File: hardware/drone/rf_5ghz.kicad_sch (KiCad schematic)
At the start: 25 parts, among them J5 Conn_01x06_Pin, U23 MM8030_2610RJ3, U7 CC3350, U8 DPX167125DT-8197B1, U9 DEA162450BT-1295A1, Y1 Crystal_GND24

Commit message: Added chip antenna footprint
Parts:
- AE1: footprint (none) -> SoftDroneLibrary:ANT-DB1-NSP250-T
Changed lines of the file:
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@@
 			)
 		)
-		(property "Footprint" ""
+		(property "Footprint" "SoftDroneLibrary:ANT-DB1-NSP250-T"
 			(at 163.83 157.48 0)
 			(hide yes)

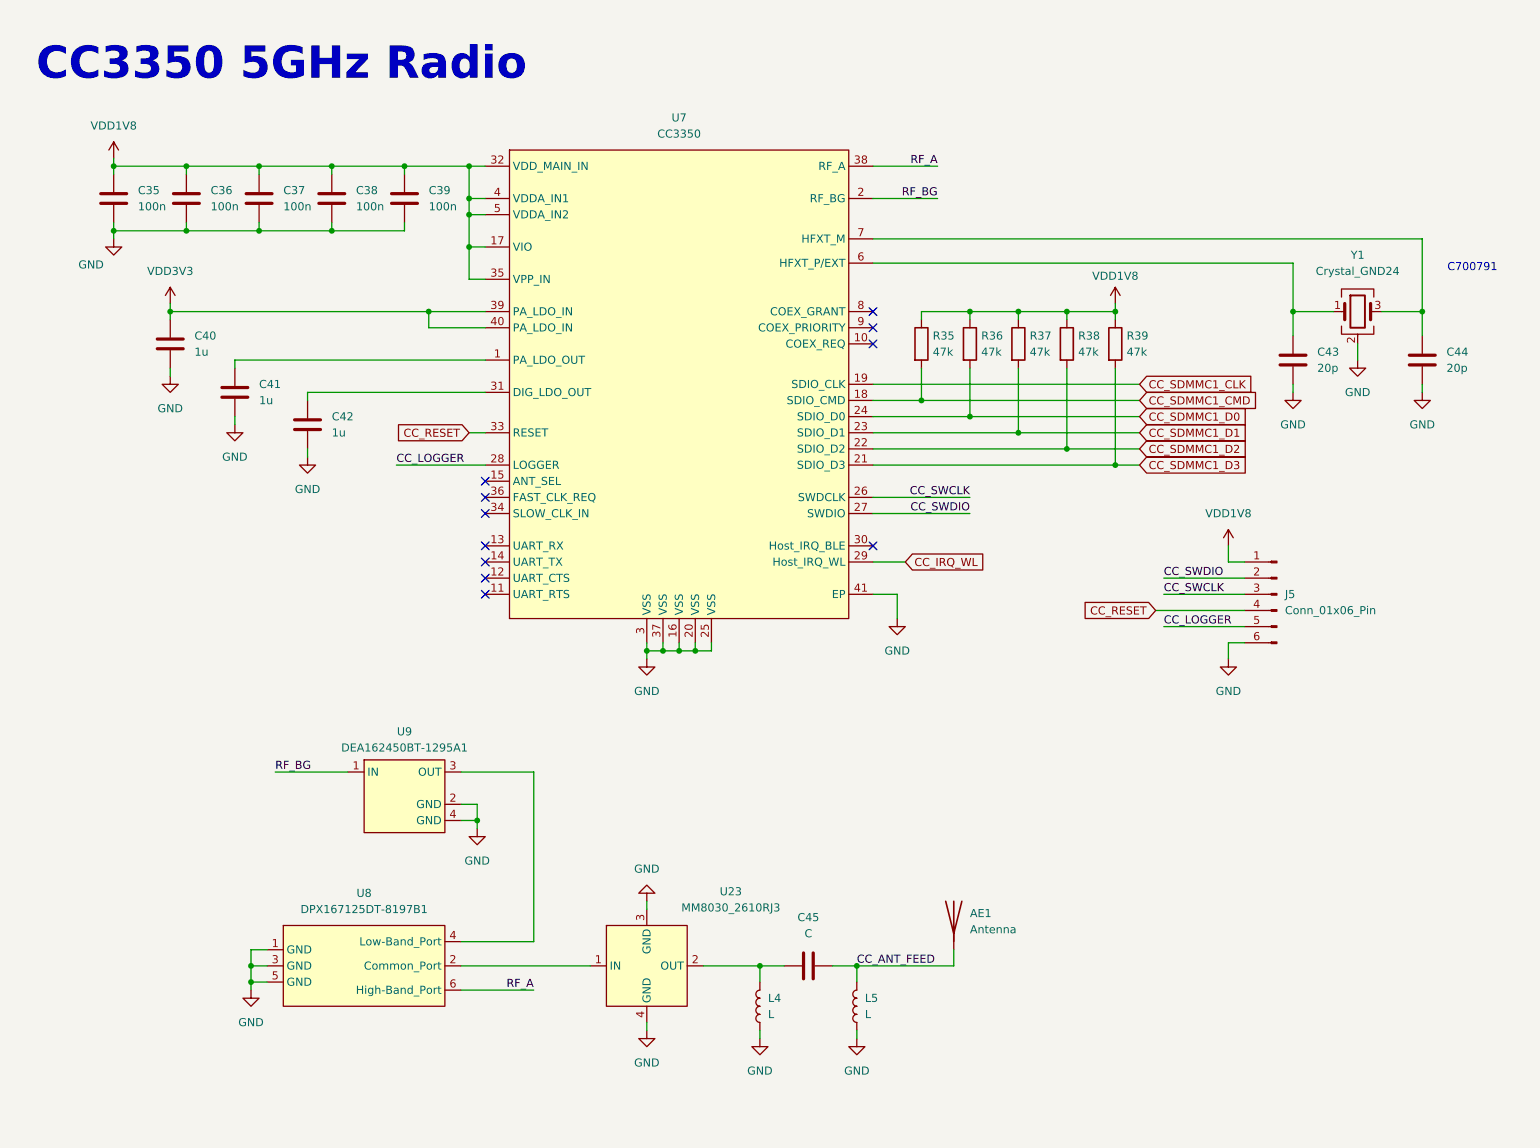
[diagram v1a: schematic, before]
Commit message: Labeled nets, added colours, and fixed stm32n6 schematic symbol issues
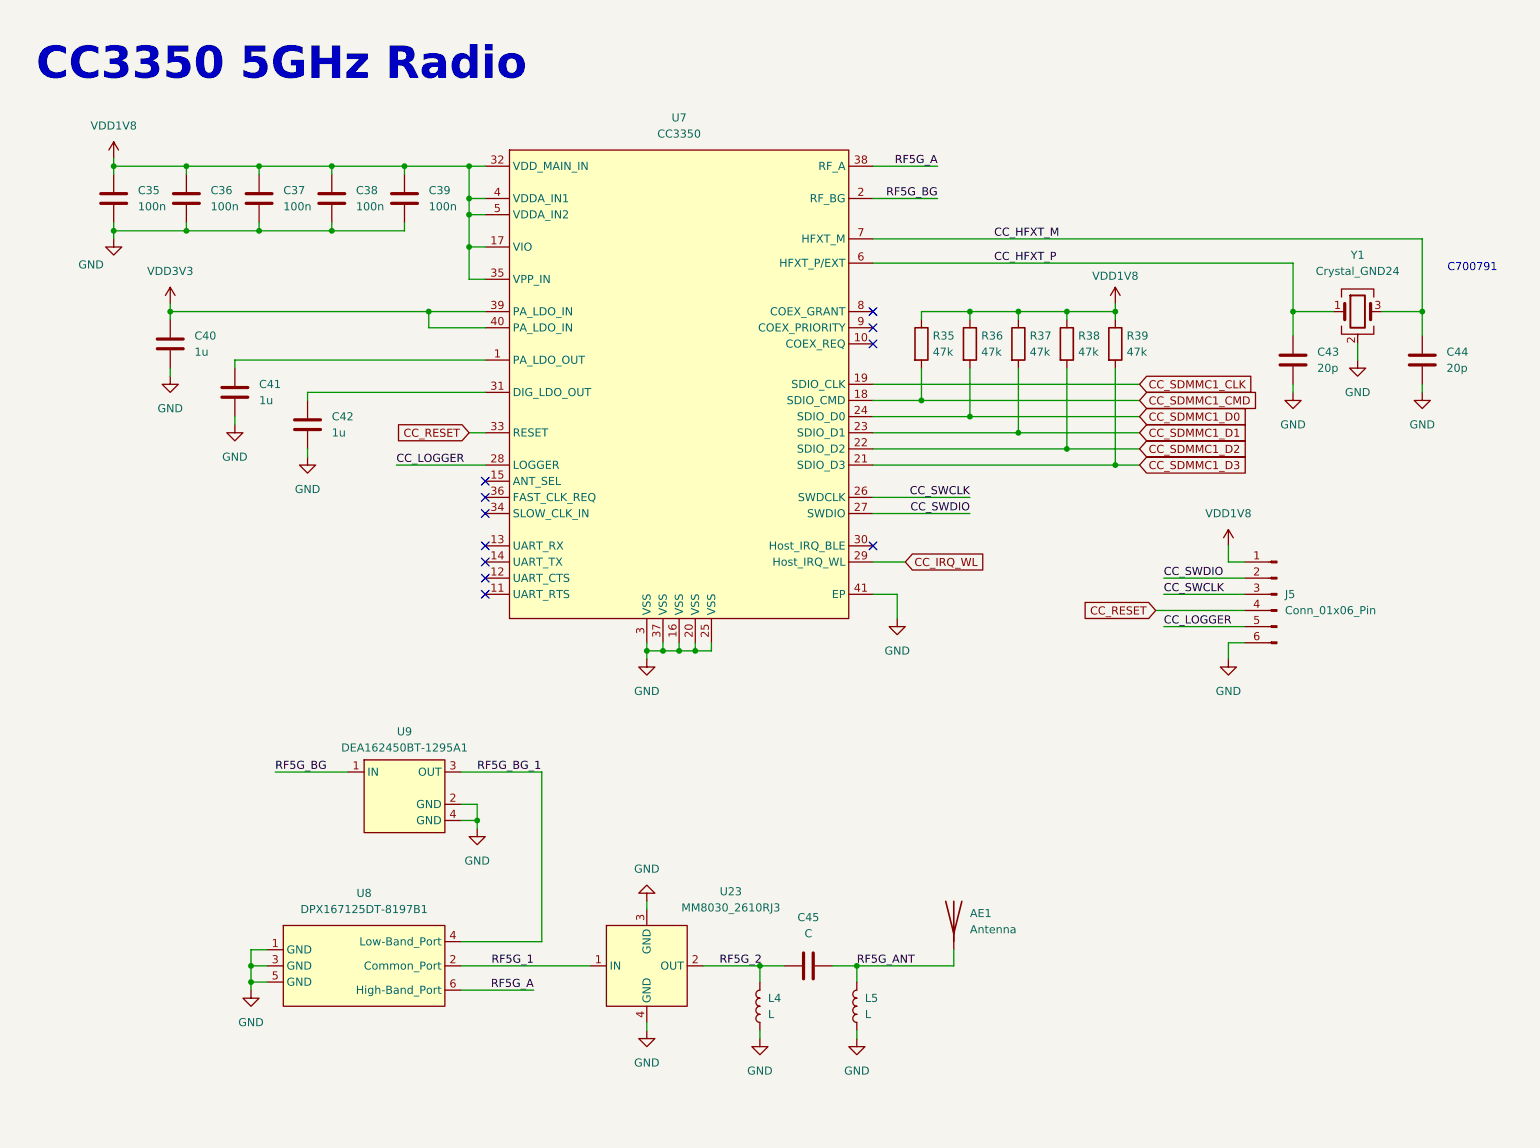
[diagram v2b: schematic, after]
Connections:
- net RF5G_BG_1: now reaches U8.4 (Low-Band_Port), U9.3 (OUT)
- net CC_HFXT_P: now reaches C43.1, U7.6 (HFXT_P/EXT), Y1.1
- net CC_HFXT_M: now reaches C44.1, U7.7 (HFXT_M), Y1.3
- net RF5G_2: now reaches C45.1, L4.2, U23.2 (OUT)
- net RF5G_1: now reaches U23.1 (IN), U8.2 (Common_Port)
- net CC_ANT_FEED renamed RF5G_ANT
- net RF_A renamed RF5G_A
- net RF_BG renamed RF5G_BG
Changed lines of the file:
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@@
 	(wire
 		(pts
-			(xy 86.36 134.62) (xy 97.79 134.62)
+			(xy 86.36 134.62) (xy 99.06 134.62)
 		)
 		(stroke
@@
 	(wire
 		(pts
-			(xy 97.79 134.62) (xy 97.79 161.29)
+			(xy 99.06 134.62) (xy 99.06 161.29)
 		)
 		(stroke
@@
 	(wire
 		(pts
-			(xy 97.79 161.29) (xy 86.36 161.29)
+			(xy 99.06 161.29) (xy 86.36 161.29)
 		)
 		(stroke
@@
 		)
 	)
-	(label "RF_A"
+	(label "CC_HFXT_M"
+		(at 170.18 50.8 0)
+		(effects
+			(font
+				(size 1.27 1.27)
+			)
+			(justify left bottom)
+		)
+	)
+	(label "RF5G_A"
 		(at 97.79 168.91 180)
 		(effects
@@
 		)
 	)
-	(label "RF_BG"
+	(label "RF5G_BG"
 		(at 161.29 44.45 180)
 		(effects
@@
 			)
 			(justify right bottom)
+		)
+	)
+	(label "RF5G_2"
+		(at 127 165.1 0)
+		(effects
+			(font
+				(size 1.27 1.27)
+			)
+			(justify left bottom)
+		)
+	)
+	(label "CC_HFXT_P"
+		(at 170.18 54.61 0)
+		(effects
+			(font
+				(size 1.27 1.27)
+			)
+			(justify left bottom)
 		)
 	)
@@
 		)
 	)
-	(label "CC_ANT_FEED"
+	(label "RF5G_BG_1"
+		(at 88.9 134.62 0)
+		(effects
+			(font
+				(size 1.27 1.27)
+			)
+			(justify left bottom)
+		)
+	)
+	(label "RF5G_ANT"
 		(at 148.59 165.1 0)
 		(effects
@@
 		)
 	)
-	(label "RF_A"
+	(label "RF5G_A"
 		(at 161.29 39.37 180)
+		(effects
+			(font
+				(size 1.27 1.27)
+			)
+			(justify right bottom)
+		)
+	)
+	(label "RF5G_1"
+		(at 97.79 165.1 180)
 		(effects
 			(font
@@
 		)
 	)
-	(label "RF_BG"
+	(label "RF5G_BG"
 		(at 57.15 134.62 0)
 		(effects

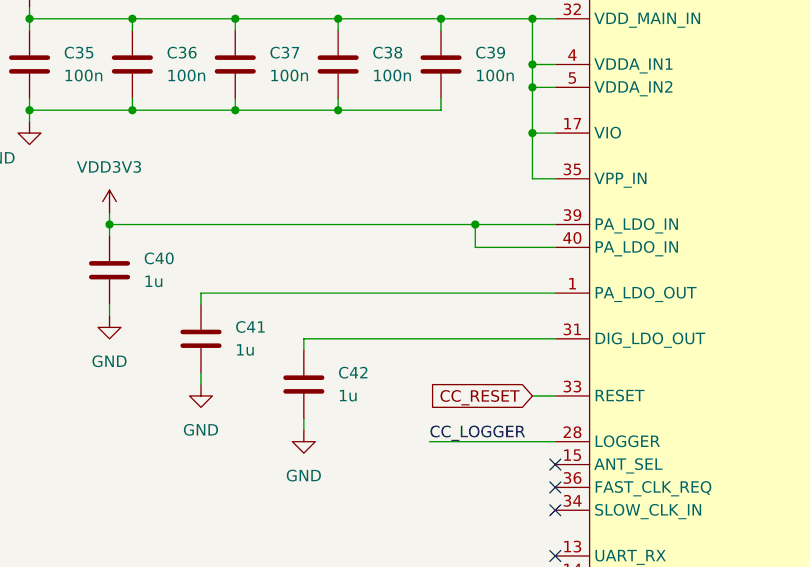
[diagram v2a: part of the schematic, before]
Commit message: Started layout and tested RF routing paths
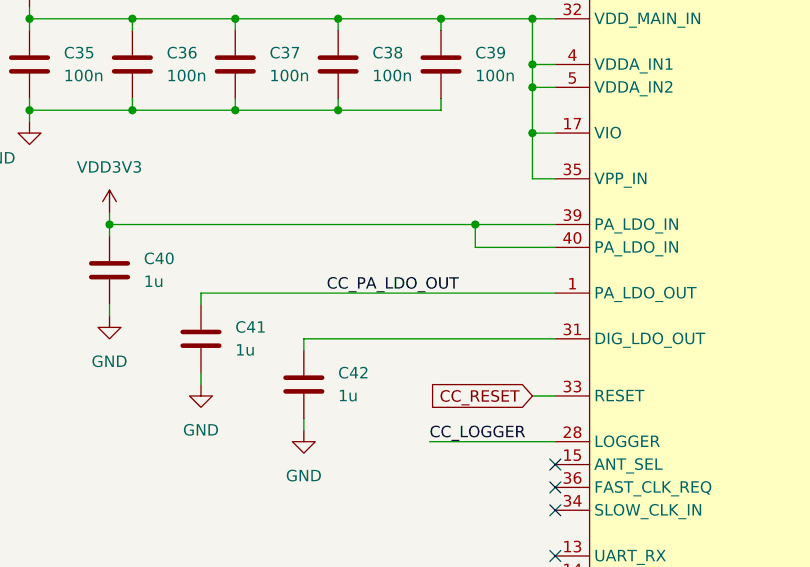
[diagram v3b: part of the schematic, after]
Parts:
- C45: footprint Capacitor_SMD:C_0402_1005Metric -> Capacitor_SMD:C_0603_1608Metric
- L4, L5: footprint Inductor_SMD:L_0402_1005Metric -> Inductor_SMD:L_0603_1608Metric
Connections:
- net CC_PA_LDO_OUT: now reaches C41.1, U7.1 (PA_LDO_OUT)
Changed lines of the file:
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@@
+		)
+	)
+	(label "CC_PA_LDO_OUT"
+		(at 64.77 69.85 0)
+		(effects
+			(font
+				(size 1.27 1.27)
+			)
+			(justify left bottom)
 		)
 	)
@@
 			)
 		)
-		(property "Footprint" "Capacitor_SMD:C_0402_1005Metric"
+		(property "Footprint" "Capacitor_SMD:C_0603_1608Metric"
 			(at 144.78 164.1348 0)
 			(hide yes)
@@
 			)
 		)
-		(property "Footprint" "Inductor_SMD:L_0402_1005Metric"
+		(property "Footprint" "Inductor_SMD:L_0603_1608Metric"
 			(at 148.59 171.45 0)
 			(hide yes)
@@
 			)
 		)
-		(property "Footprint" "Inductor_SMD:L_0402_1005Metric"
+		(property "Footprint" "Inductor_SMD:L_0603_1608Metric"
 			(at 133.35 171.45 0)
 			(hide yes)

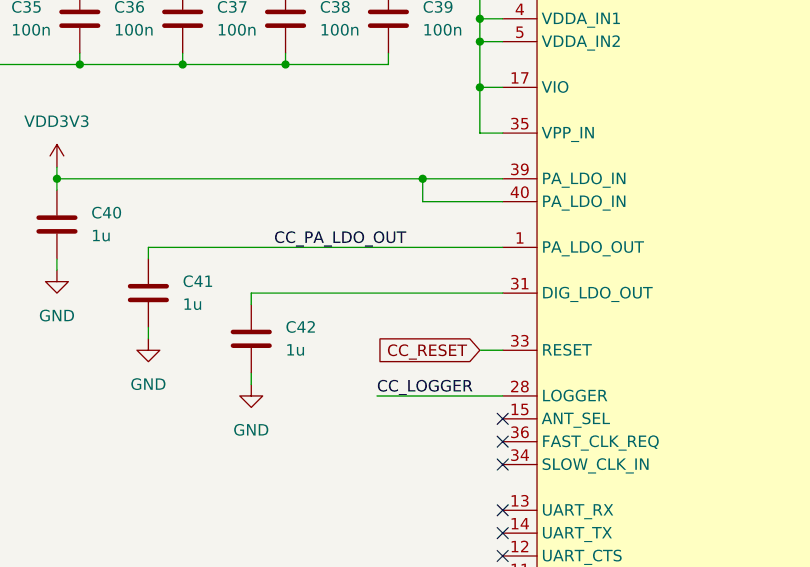
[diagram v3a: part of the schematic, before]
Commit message: Routed CC3350 RF, SDMMC, decoupling and crystal
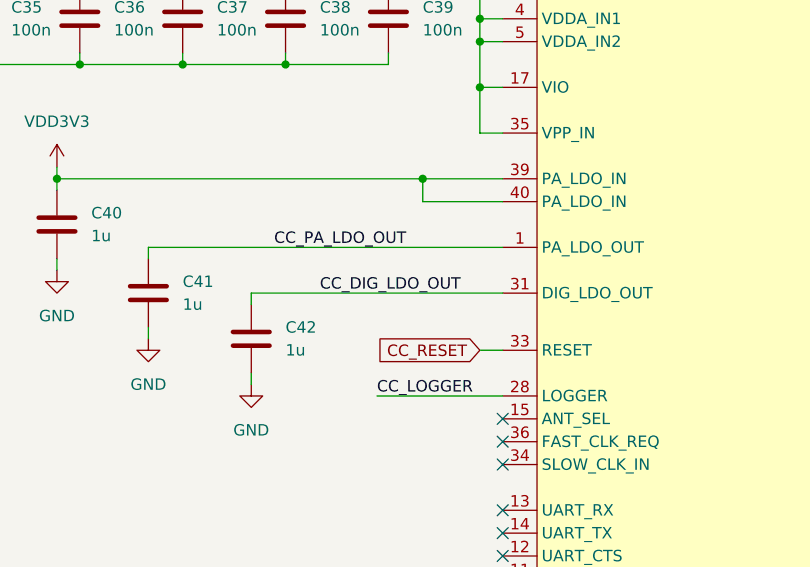
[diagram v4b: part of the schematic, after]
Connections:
- net CC_DIG_LDO_OUT: now reaches C42.1, U7.31 (DIG_LDO_OUT)
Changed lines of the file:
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@@
+		)
+	)
+	(label "CC_DIG_LDO_OUT"
+		(at 69.85 74.93 0)
+		(effects
+			(font
+				(size 1.27 1.27)
+			)
+			(justify left bottom)
 		)
 	)

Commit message: More CC3350 routing
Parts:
- R35, R36, R37, R38, R39: footprint Resistor_SMD:R_0402_1005Metric -> Resistor_SMD:R_0201_0603Metric
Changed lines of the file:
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@@
 			)
 		)
-		(property "Footprint" "Resistor_SMD:R_0402_1005Metric"
+		(property "Footprint" "Resistor_SMD:R_0201_0603Metric"
 			(at 156.972 67.31 90)
 			(hide yes)
@@
 			)
 		)
-		(property "Footprint" "Resistor_SMD:R_0402_1005Metric"
+		(property "Footprint" "Resistor_SMD:R_0201_0603Metric"
 			(at 179.832 67.31 90)
 			(hide yes)
@@
 			)
 		)
-		(property "Footprint" "Resistor_SMD:R_0402_1005Metric"
+		(property "Footprint" "Resistor_SMD:R_0201_0603Metric"
 			(at 164.592 67.31 90)
 			(hide yes)
@@
 			)
 		)
-		(property "Footprint" "Resistor_SMD:R_0402_1005Metric"
+		(property "Footprint" "Resistor_SMD:R_0201_0603Metric"
 			(at 187.452 67.31 90)
 			(hide yes)
@@
 			)
 		)
-		(property "Footprint" "Resistor_SMD:R_0402_1005Metric"
+		(property "Footprint" "Resistor_SMD:R_0201_0603Metric"
 			(at 172.212 67.31 90)
 			(hide yes)

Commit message: Small cleanup and more power routing
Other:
- note added: "Diplexer + RF Filter"
- moved on the sheet: AE1, C45, L4, L5, U23, U8, U9

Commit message: Schematic cleanup and changed pi network footprints
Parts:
- C45: value C -> 10p; footprint Capacitor_SMD:C_0603_1608Metric -> Capacitor_SMD:C_0402_1005Metric
- L4, L5: footprint Inductor_SMD:L_0603_1608Metric -> Inductor_SMD:L_0402_1005Metric; now not fitted
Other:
- note added: "TI CC335x Revised October 2025 values"
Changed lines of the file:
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@@
 		)
 	)
+	(text "TI CC335x Revised October 2025 values"
+		(exclude_from_sim no)
+		(at 145.542 157.48 0)
+		(effects
+			(font
+				(size 0.889 0.889)
+			)
+		)
+	)
 	(text "Diplexer + RF Filter"
 		(exclude_from_sim no)
@@
 			)
 		)
-		(property "Value" "C"
+		(property "Value" "10p"
 			(at 137.16 166.37 90)
 			(show_name no)
@@
 			)
 		)
-		(property "Footprint" "Capacitor_SMD:C_0603_1608Metric"
+		(property "Footprint" "Capacitor_SMD:C_0402_1005Metric"
 			(at 140.97 170.4848 0)
 			(hide yes)
@@
 		(on_board yes)
 		(in_pos_files yes)
-		(dnp no)
+		(dnp yes)
 		(fields_autoplaced yes)
 		(property "Reference" "L5"
@@
 			)
 		)
-		(property "Footprint" "Inductor_SMD:L_0603_1608Metric"
+		(property "Footprint" "Inductor_SMD:L_0402_1005Metric"
 			(at 144.78 177.8 0)
 			(hide yes)
@@
 		(on_board yes)
 		(in_pos_files yes)
-		(dnp no)
+		(dnp yes)
 		(fields_autoplaced yes)
 		(property "Reference" "L4"
@@
 			)
 		)
-		(property "Footprint" "Inductor_SMD:L_0603_1608Metric"
+		(property "Footprint" "Inductor_SMD:L_0402_1005Metric"
 			(at 129.54 177.8 0)
 			(hide yes)
